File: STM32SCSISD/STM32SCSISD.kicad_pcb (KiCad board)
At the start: 2 copper layers, 43.2 x 91.4 mm, 41 parts, among them J7 Micro_SD_Card_Det_Hirose_DM3AT, U1 STM32F103C8Tx, U2 MIC5504-3.3YM5, Y1 8MHz

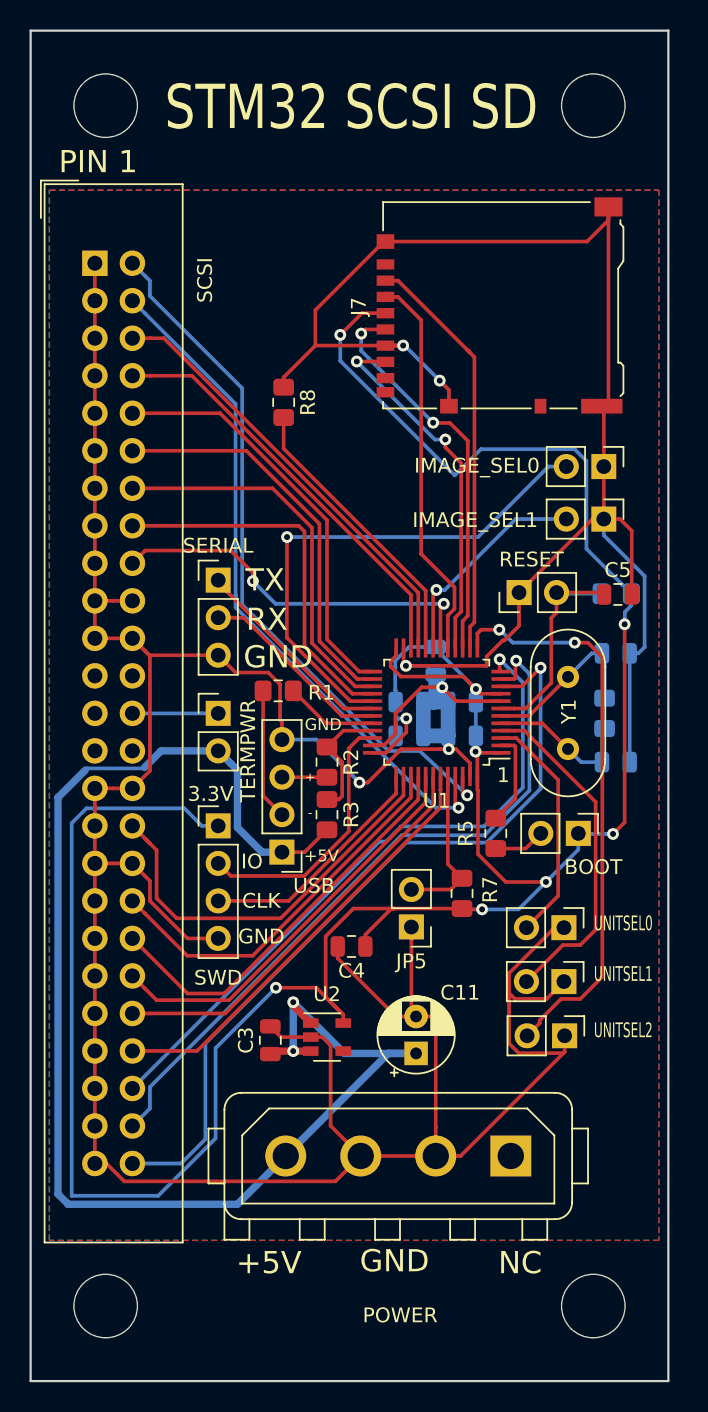
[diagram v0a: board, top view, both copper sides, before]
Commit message: Fixed the layout so that now it in sync with schematic. DB0 and DB1 is now corrected.
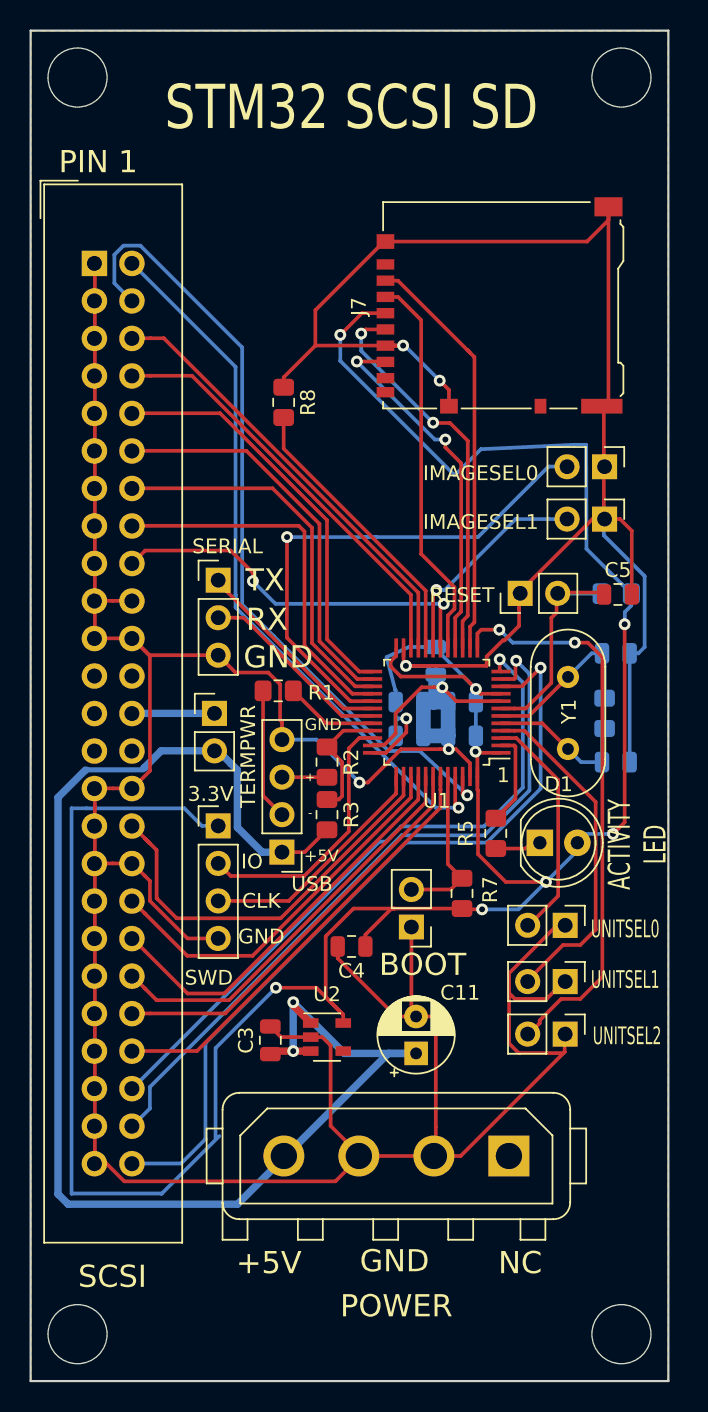
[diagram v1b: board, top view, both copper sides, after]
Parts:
- removed ? (x4): MountingHole_4.3mm_M4, MountingHole:MountingHole_4.3mm_M4
- removed BOOT: ACTIVITYLED, Connector_PinHeader_2.54mm:PinHeader_1x02_P2.54mm_Vertical
- removed IMAGE_SEL0: IMAGE_SEL0, Connector_PinHeader_2.54mm:PinHeader_1x02_P2.54mm_Vertical
- removed IMAGE_SEL1: IMAGE_SEL1, Connector_PinHeader_2.54mm:PinHeader_1x02_P2.54mm_Vertical
- removed POWER: AMP FLOPPY PWR, General:TE_MATE-N-LOK_350211-1_1x04_P5.08mm_Vertical
- removed RESET: RESET, Connector_PinHeader_2.54mm:PinHeader_1x02_P2.54mm_Vertical
- removed SCSI: SCSI, Connector_IDC:IDC-Header_2x25_P2.54mm_Vertical
- removed SERIAL: SERIAL_DEBUG, Connector_PinHeader_2.54mm:PinHeader_1x03_P2.54mm_Vertical
- removed SWD: SWD, Connector_PinHeader_2.54mm:PinHeader_1x04_P2.54mm_Vertical
- removed TERMPWR: TERMPWR_SUPPLY, Connector_PinHeader_2.54mm:PinHeader_1x02_P2.54mm_Vertical
- removed UNITSEL0: UNITSEL0, Connector_PinHeader_2.54mm:PinHeader_1x02_P2.54mm_Vertical
- removed UNITSEL1: UNITSEL1, Connector_PinHeader_2.54mm:PinHeader_1x02_P2.54mm_Vertical
- removed UNITSEL2: UNITSEL2, Connector_PinHeader_2.54mm:PinHeader_1x02_P2.54mm_Vertical
- removed USB: USB, Connector_PinHeader_2.54mm:PinHeader_1x04_P2.54mm_Vertical
- added D1: ACTIVITY LED, LED_THT:LED_D5.0mm, F.Cu at (98.0, 93.1)
- added J1: SERIAL_DEBUG, Connector_PinHeader_2.54mm:PinHeader_1x03_P2.54mm_Vertical, F.Cu at (76.2, 75.3)
- added J2: SWD, Connector_PinHeader_2.54mm:PinHeader_1x04_P2.54mm_Vertical, F.Cu at (76.2, 91.9)
- added J3: USB, Connector_PinHeader_2.54mm:PinHeader_1x04_P2.54mm_Vertical, F.Cu at (80.5, 93.7)
- added J4: SCSI, Connector_IDC:IDC-Header_2x25_P2.54mm_Vertical, F.Cu at (67.8, 53.9)
- added J6: AMP FLOPPY PWR, General:TE_MATE-N-LOK_350211-1_1x04_P5.08mm_Vertical, F.Cu at (95.9, 114.3)
- added JP1: IMAGE_SEL0, Connector_PinHeader_2.54mm:PinHeader_1x02_P2.54mm_Vertical, F.Cu at (102.4, 67.6)
- added JP2: IMAGE_SEL1, Connector_PinHeader_2.54mm:PinHeader_1x02_P2.54mm_Vertical, F.Cu at (102.4, 71.2)
- added JP3: UNITSEL2, Connector_PinHeader_2.54mm:PinHeader_1x02_P2.54mm_Vertical, F.Cu at (99.7, 106.0)
- added JP4: TERMPWR_SUPPLY, Connector_PinHeader_2.54mm:PinHeader_1x02_P2.54mm_Vertical, F.Cu at (75.9, 84.3)
- added JP6: RESET, Connector_PinHeader_2.54mm:PinHeader_1x02_P2.54mm_Vertical, F.Cu at (96.6, 76.2)
- added JP7: UNITSEL0, Connector_PinHeader_2.54mm:PinHeader_1x02_P2.54mm_Vertical, F.Cu at (99.7, 98.7)
- added JP8: UNITSEL1, Connector_PinHeader_2.54mm:PinHeader_1x02_P2.54mm_Vertical, F.Cu at (99.7, 102.5)
- added REF**: MountingHole_4mm, MountingHole:MountingHole_4mm, F.Cu at (66.7, 41.3)
- added REF**: MountingHole_4mm, MountingHole:MountingHole_4mm, F.Cu at (103.5, 41.3)
- added REF**: MountingHole_4mm, MountingHole:MountingHole_4mm, F.Cu at (103.5, 126.4)
- added REF**: MountingHole_4mm, MountingHole:MountingHole_4mm, F.Cu at (66.7, 126.4)
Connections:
- U1 pad 45: /SCSI_DB1 -> /SCSI_DB0
- U1 pad 46: /SCSI_DB0 -> /SCSI_DB1
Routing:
- net /SCSI_DB1: track 46.8 -> 55.0 mm
- net +3V3: track 195.7 -> 197.9 mm
- net /SCSI_DB0: track 48.2 -> 49.2 mm
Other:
- board text added: "ACTIVITY LED"
- board text added: "BOOT"
- board text added: "IMAGESEL0"
- board text added: "IMAGESEL1"
- board text added: "POWER"
- board text added: "RESET"
- board text added: "SCSI"
- board text added: "SERIAL"
- board text added: "SWD"
- board text added: "TERMPWR"
- board text added: "UNITSEL0"
- board text added: "UNITSEL1"
- board text added: "UNITSEL2"
- board text added: "USB"

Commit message: Moved the mounting holes a bit and made sure the filled area didn't enter the area of the mounting holes.
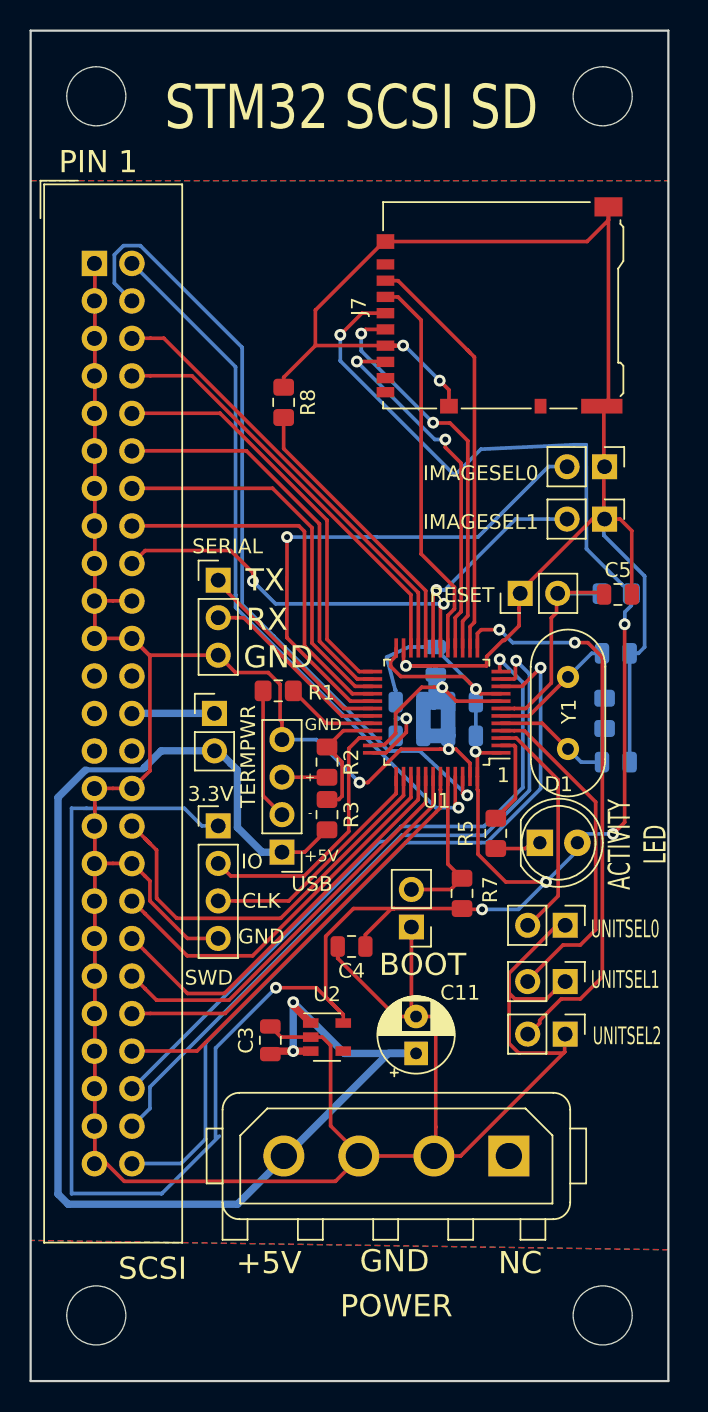
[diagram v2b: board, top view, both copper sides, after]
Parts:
- moved REF** 1.80 mm to (67.9, 42.5)
- moved REF** 1.80 mm to (102.2, 42.5)
- moved REF** 1.80 mm to (102.2, 125.1)
- moved REF** 1.80 mm to (67.9, 125.1)
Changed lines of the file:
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@@
   )
   (module MountingHole:MountingHole_4mm (layer F.Cu)
-    (at 66.675 41.275)
+    (at 67.945 42.545)
     (descr "Mounting Hole 4mm, no annular")
     (tags "mounting hole 4mm no annular")
@@
   )
   (module MountingHole:MountingHole_4mm (layer F.Cu)
-    (at 103.505 41.275)
+    (at 102.235 42.545)
     (descr "Mounting Hole 4mm, no annular")
     (tags "mounting hole 4mm no annular")
@@
   )
   (module MountingHole:MountingHole_4mm (layer F.Cu)
-    (at 103.505 126.365)
+    (at 102.235 125.095)
     (descr "Mounting Hole 4mm, no annular")
     (tags "mounting hole 4mm no annular")
@@
   )
   (module MountingHole:MountingHole_4mm (layer F.Cu)
-    (at 66.675 126.365)
+    (at 67.945 125.095)
     (descr "Mounting Hole 4mm, no annular")
     (tags "mounting hole 4mm no annular")
@@
     (pad 1 np_thru_hole circle (at 0 0) (size 4 4) (drill 4) (layers *.Cu *.Mask))
   )
-  (gr_text SCSI (at 69.0372 122.4661) (layer F.SilkS)
+  (gr_text SCSI (at 71.755 121.92) (layer F.SilkS)
     (effects (font (size 1.5 1.5) (thickness 0.3)))
   )
@@
   (segment (start 80.527 88.655) (end 80.518 88.646) (width 0.25) (layer F.Cu) (net 12))
   (segment (start 83.566 88.655) (end 80.527 88.655) (width 0.25) (layer F.Cu) (net 12))
-  (segment (start 92.75 89.781085) (end 92.75 88.6) (width 0.25) (layer F.Cu) (net 14))
-  (segment (start 93.0656 89.8779) (end 92.75 89.781085) (width 0.25) (layer F.Cu) (net 14))
-  (via (at 93.0656 89.8779) (size 0.8) (drill 0.4) (layers F.Cu B.Cu) (net 14))
   (via (at 92.475 90.7161) (size 0.8) (drill 0.4) (layers F.Cu B.Cu) (net 13))
   (segment (start 92.25 90.4911) (end 92.475 90.7161) (width 0.25) (layer F.Cu) (net 13))
@@
   (segment (start 77.375001 60.865001) (end 70.485 53.975) (width 0.25) (layer B.Cu) (net 13))
   (segment (start 77.375001 76.2889) (end 77.375001 60.865001) (width 0.25) (layer B.Cu) (net 13))
+  (segment (start 92.75 89.781085) (end 92.75 88.6) (width 0.25) (layer F.Cu) (net 14))
+  (segment (start 93.0656 89.8779) (end 92.75 89.781085) (width 0.25) (layer F.Cu) (net 14))
+  (via (at 93.0656 89.8779) (size 0.8) (drill 0.4) (layers F.Cu B.Cu) (net 14))
   (segment (start 69.169399 55.199399) (end 70.485 56.515) (width 0.25) (layer B.Cu) (net 14))
   (segment (start 79.953101 79.092951) (end 79.953101 79.089501) (width 0.25) (layer B.Cu) (net 14))
@@
   (segment (start 96.767773 82.5) (end 95.35 82.5) (width 0.25) (layer F.Cu) (net 31))
   (segment (start 98.0302 81.237573) (end 96.767773 82.5) (width 0.25) (layer F.Cu) (net 31))
-  (segment (start 97.019 93.481) (end 98.044 92.456) (width 0.25) (layer F.Cu) (net 57))
-  (segment (start 94.996 93.481) (end 97.019 93.481) (width 0.25) (layer F.Cu) (net 57))
   (segment (start 88.375 55.0305) (end 87.525 55.0305) (width 0.25) (layer F.Cu) (net 32))
   (segment (start 93.550031 78.160569) (end 93.550031 60.205531) (width 0.25) (layer F.Cu) (net 32))
@@
   (segment (start 96.339874 71.172211) (end 98.567608 71.172211) (width 0.25) (layer B.Cu) (net 45))
   (segment (start 90.975 75.9714) (end 91.540685 75.9714) (width 0.25) (layer B.Cu) (net 45))
+  (segment (start 97.019 93.481) (end 98.044 92.456) (width 0.25) (layer F.Cu) (net 57))
+  (segment (start 94.996 93.481) (end 97.019 93.481) (width 0.25) (layer F.Cu) (net 57))
   (zone (net 2) (net_name GND) (layer F.Cu) (hatch edge 0.508)
     (connect_pads (clearance 0.508))
@@
     (polygon
       (pts
-        (xy 63.5 38.1) (xy 106.68 38.1) (xy 106.68 129.54) (xy 63.5 129.54)
+        (xy 64.135 48.26) (xy 106.68 48.26) (xy 106.68 120.65) (xy 63.5 120.015) (xy 63.5 48.26)
       )
     )
@@
     (polygon
       (pts
-        (xy 63.5 38.1) (xy 106.68 38.1) (xy 106.68 129.54) (xy 63.5 129.54)
+        (xy 63.5 48.26) (xy 106.68 48.26) (xy 106.68 120.65) (xy 63.5 120.015)
       )
     )

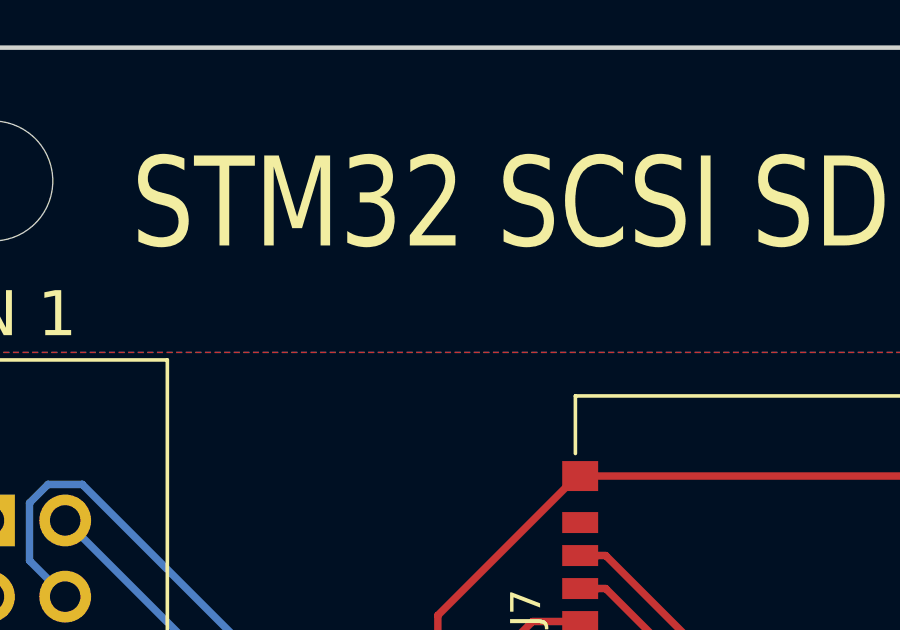
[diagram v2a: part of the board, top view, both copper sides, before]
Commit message: Added version  1.1 in the silkscreen.
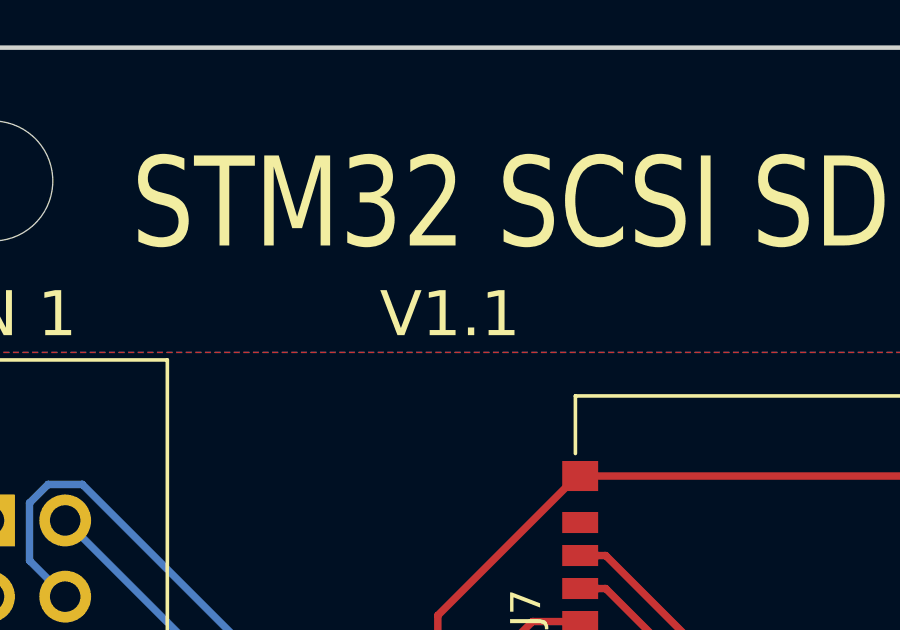
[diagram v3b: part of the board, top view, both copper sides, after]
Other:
- board text added: "V1.1"
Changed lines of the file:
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@@
   (general
     (thickness 1.6)
-    (drawings 38)
+    (drawings 39)
     (tracks 543)
     (zones 0)
@@
     (pad 1 np_thru_hole circle (at 0 0) (size 4 4) (drill 4) (layers *.Cu *.Mask))
   )
+  (gr_text V1.1 (at 83.185 46.99) (layer F.SilkS)
+    (effects (font (size 1.5 1.5) (thickness 0.3)))
+  )
   (gr_text SCSI (at 71.755 121.92) (layer F.SilkS)
